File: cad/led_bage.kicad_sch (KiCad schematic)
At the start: 3233 parts, among them J1 Conn_01x08_Socket, J2 Conn_01x10_MountingPin, U1 SI7145DP-T1-GE3, U2 74AHCT1G125, U3 74AHCT1G125, U4 74AHCT1G125, U5 74AHCT1G125, U6 74AHCT1G125, U7 74AHCT1G125, U8 74AHCT1G125, U9 74AHCT1G125

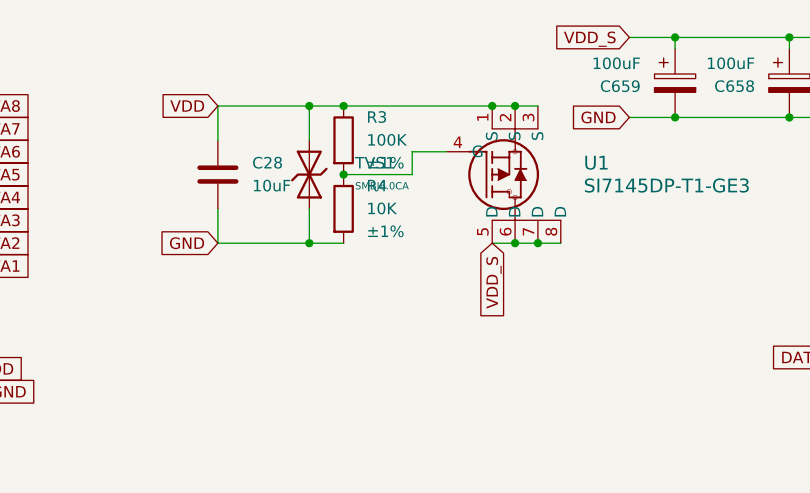
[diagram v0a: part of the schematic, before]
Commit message: fix(cad): put U1 drain on the input so reverse polarity is blocked
The P-FET was wired source-on-input, so its body diode conducted with a
reversed plug and the protection did nothing. Drain (pins 5-8 + EP) now
goes to VDD, source (pins 1-3) to VDD_S, R3 sits between gate and source.
The fabricated 100-LED sample still has the old wiring.
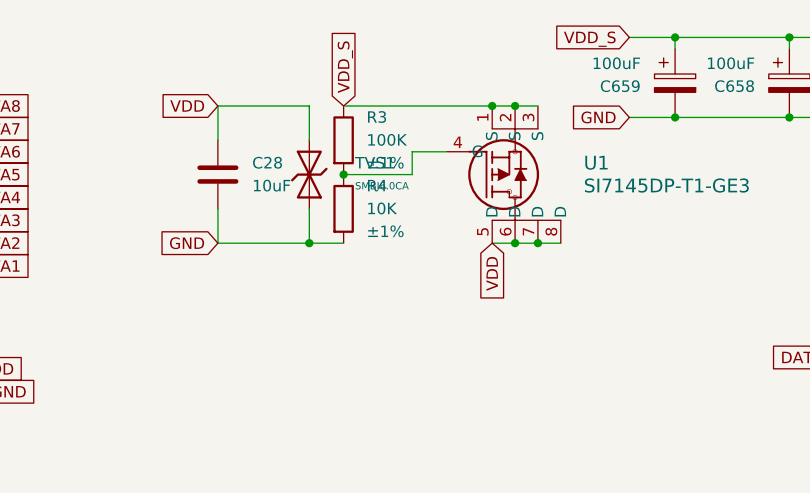
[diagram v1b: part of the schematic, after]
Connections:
- net VDD: now also U1.5 (D), U1.6 (D), U1.7 (D), U1.8 (D); no longer R3.1, U1.1 (S), U1.2 (S), U1.3 (S)
- net VDD_S: now also R3.1, U1.1 (S), U1.2 (S), U1.3 (S); no longer U1.5 (D), U1.6 (D), U1.7 (D), U1.8 (D)
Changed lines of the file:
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@@
 	)
 	(junction
-		(at -57.15 10.16)
-		(diameter 0)
-		(color 0 0 0 0)
-	)
-	(junction
 		(at 435.61 45.72)
 		(diameter 0)
@@
 	)
 	(junction
-		(at -53.34 10.16)
-		(diameter 0)
-		(color 0 0 0 0)
-	)
-	(junction
 		(at 4607.56 45.72)
 		(diameter 0)
@@
 	(wire
 		(pts
-			(xy -57.15 10.16) (xy -53.34 10.16)
-		)
-		(stroke
-			(width 0)
-			(type default)
-		)
-	)
-	(wire
-		(pts
 			(xy 2964.18 200.66) (xy 2980.69 200.66)
 		)
@@
 		)
 	)
+	(global_label "VDD_S"
+		(shape input)
+		(at -53.34 10.16 90)
+		(fields_autoplaced yes)
+		(effects
+			(font
+				(size 1.27 1.27)
+			)
+			(justify left)
+		)
+		(property "Intersheetrefs" "${INTERSHEET_REFS}"
+			(at -53.34 1.3691 90)
+			(hide yes)
+			(show_name no)
+			(do_not_autoplace no)
+			(effects
+				(font
+					(size 1.27 1.27)
+				)
+				(justify left)
+			)
+		)
+	)
 	(global_label "GND"
 		(shape input)
@@
 		)
 	)
-	(global_label "VDD_S"
+	(global_label "VDD"
 		(shape input)
 		(at -36.83 25.4 270)
